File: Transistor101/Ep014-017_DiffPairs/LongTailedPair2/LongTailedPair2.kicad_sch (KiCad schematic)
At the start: 17 parts, among them J1 AWG channel 1, J2 AWG channel 2, J3 Output to oscilloscope, Q1 DMMT5551, Q2 DMMT5551, T1 SEE NOTES

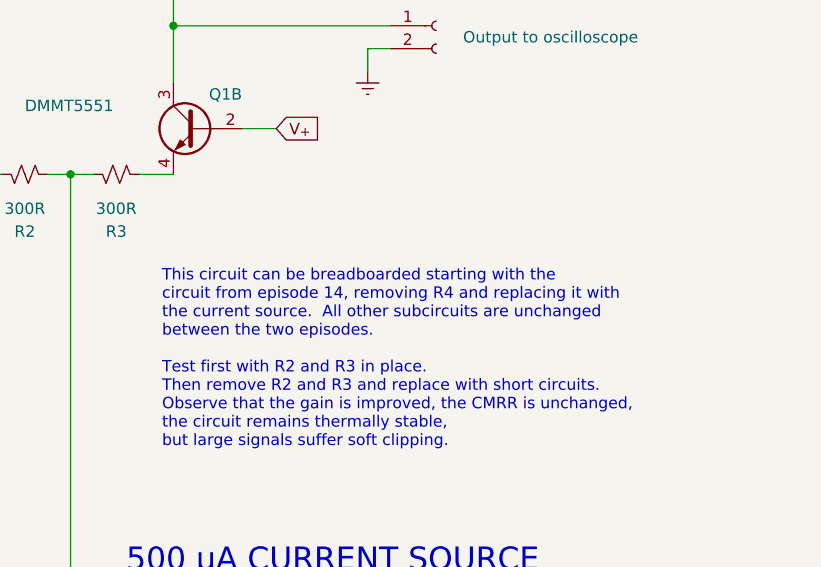
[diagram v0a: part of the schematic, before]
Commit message: Typos in notes on schematic
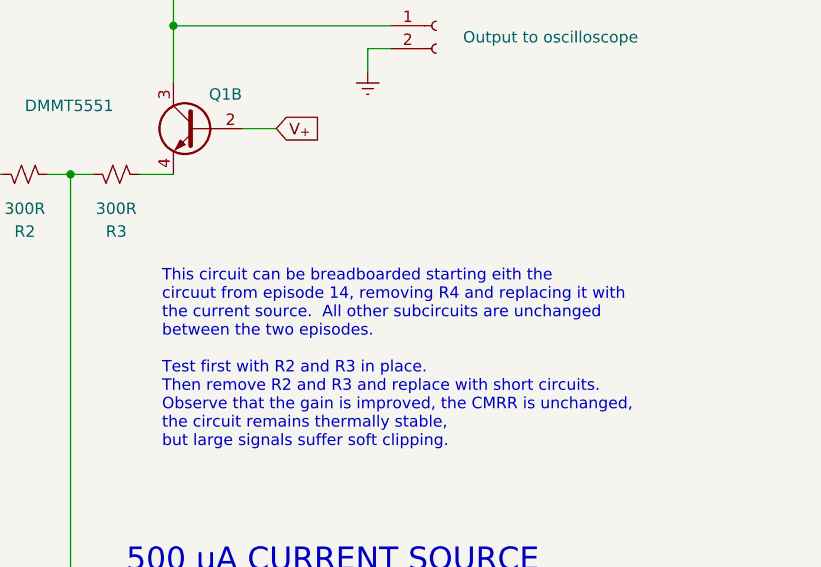
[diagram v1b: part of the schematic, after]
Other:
- note added: "This circuit can be breadboarded starting eith the circuut from episode 14, removing R4 and replacing it with the current source. All other subcircuits are unchanged between the two episodes. Test first with R2 and R3 in place. Then remove R2 and R3 and replace with short circuits. Observe that the gain is improved, the CMRR is unchanged, the circuit remains thermally stable, but large signals su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"
- note removed: "This circuit can be breadboarded starting with the circuit from episode 14, removing R4 and replacing it with the current source. All other subcircuits are unchanged between the two episodes. Test first with R2 and R3 in place. Then remove R2 and R3 and replace with short circuits. Observe that the gain is improved, the CMRR is unchanged, the circuit remains thermally stable, but large signals su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"
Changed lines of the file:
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@@
     (effects (font (size 2.54 2.54)) (justify right bottom))
   )
-  (text "This circuit can be breadboarded starting with the\ncircuit from episode 14, removing R4 and replacing it with\nthe current source.  All other subcircuits are unchanged\nbetween the two episodes.\n\nTest first with R2 and R3 in place.\nThen remove R2 and R3 and replace with short circuits.\nObserve that the gain is improved, the CMRR is unchanged,\nthe circuit remains thermally stable,\nbut large signals suffer soft clipping."
+  (text "This circuit can be breadboarded starting eith the\ncircuut from episode 14, removing R4 and replacing it with\nthe current source.  All other subcircuits are unchanged\nbetween the two episodes.\n\nTest first with R2 and R3 in place.\nThen remove R2 and R3 and replace with short circuits.\nObserve that the gain is improved, the CMRR is unchanged,\nthe circuit remains thermally stable,\nbut large signals suffer soft clipping."
     (at 172.72 107.95 0)
     (effects (font (size 1.27 1.27)) (justify left bottom))
